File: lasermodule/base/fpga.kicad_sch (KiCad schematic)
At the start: 20 parts, among them U12 ICE40UP5K-SG48ITR-FPGA_Lattice, U13 S25FL064LABMFI010, U14 MCP1700x-120xxTT

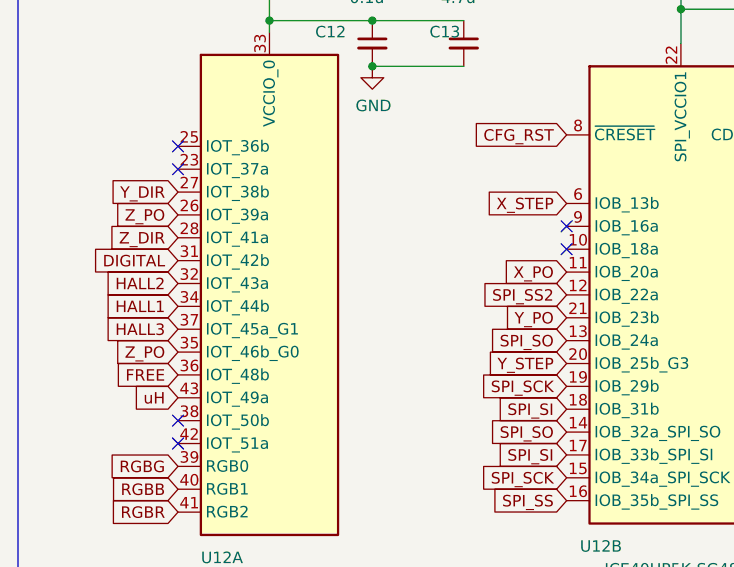
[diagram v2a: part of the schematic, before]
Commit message: flatex cable increased from 15 to 20 pins
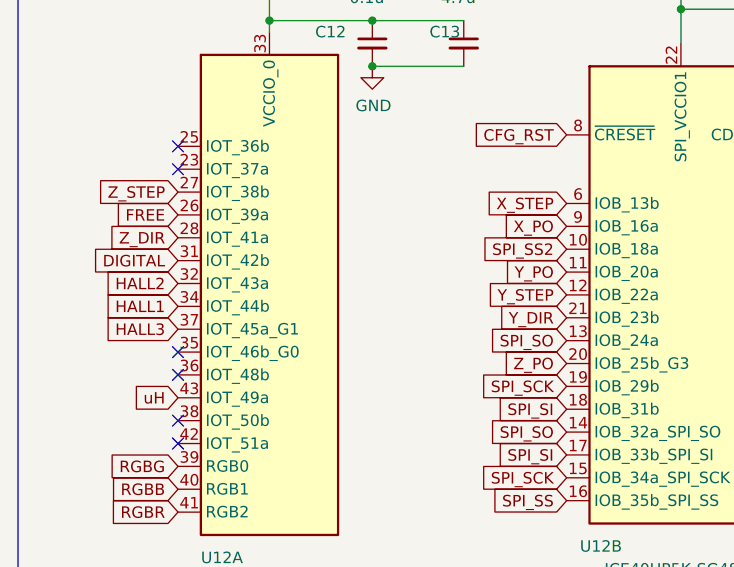
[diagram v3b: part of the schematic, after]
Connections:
- net FREE: now also U12.26 (IOT_39a); no longer U12.36 (IOT_48b)
- net SPI_SS2: now also U12.10 (IOB_18a); no longer U12.12 (IOB_22a)
- net X_PO: now also U12.9 (IOB_16a); no longer U12.11 (IOB_20a)
- net Y_DIR: now also U12.21 (IOB_23b); no longer U12.27 (IOT_38b)
- net Y_PO: now also U12.11 (IOB_20a); no longer U12.21 (IOB_23b)
- net Y_STEP: now also U12.12 (IOB_22a); no longer U12.20 (IOB_25b_G3)
- net Z_PO: now also U12.20 (IOB_25b_G3); no longer U12.26 (IOT_39a), U12.35 (IOT_46b_G0)
- new net Z_STEP: U12.27 (IOT_38b)
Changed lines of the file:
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@@
   )
   (no_connect (at 80.01 54.61))
-  (no_connect (at 123.19 60.96))
+  (no_connect (at 80.01 77.47))
   (no_connect (at 80.01 85.09))
   (no_connect (at 80.01 52.07))
   (no_connect (at 80.01 82.55))
-  (no_connect (at 123.19 63.5))
+  (no_connect (at 80.01 74.93))
   (wire (pts (xy 111.76 43.18) (xy 101.6 43.18))
     (stroke (width 0) (type default))
@@
     (effects (font (size 3 3)) (justify left bottom))
   )
-  (global_label "Y_STEP" (shape input) (at 123.19 76.2 180) (fields_autoplaced)
-    (effects (font (size 1.27 1.27)) (justify right))
-    (property "Intersheetrefs" "${INTERSHEET_REFS}" (at 114.2861 76.2 0)
+  (global_label "Y_STEP" (shape input) (at 123.19 68.58 180) (fields_autoplaced)
+    (effects (font (size 1.27 1.27)) (justify right))
+    (property "Intersheetrefs" "${INTERSHEET_REFS}" (at 114.2861 68.58 0)
       (effects (font (size 1.27 1.27)) (justify right) hide)
     )
@@
     )
   )
-  (global_label "SPI_SS2" (shape input) (at 123.19 68.58 180) (fields_autoplaced)
-    (effects (font (size 1.27 1.27)) (justify right))
-    (property "Intersheetrefs" "${INTERSHEET_REFS}" (at 113.1853 68.5006 0)
+  (global_label "SPI_SS2" (shape input) (at 123.19 63.5 180) (fields_autoplaced)
+    (effects (font (size 1.27 1.27)) (justify right))
+    (property "Intersheetrefs" "${INTERSHEET_REFS}" (at 113.1853 63.4206 0)
       (effects (font (size 1.27 1.27)) (justify right) hide)
     )
@@
     )
   )
-  (global_label "X_PO" (shape input) (at 123.19 66.04 180) (fields_autoplaced)
-    (effects (font (size 1.27 1.27)) (justify right))
-    (property "Intersheetrefs" "${INTERSHEET_REFS}" (at -121.92 6.35 0)
+  (global_label "X_PO" (shape input) (at 123.19 60.96 180) (fields_autoplaced)
+    (effects (font (size 1.27 1.27)) (justify right))
+    (property "Intersheetrefs" "${INTERSHEET_REFS}" (at -121.92 1.27 0)
       (effects (font (size 1.27 1.27)) hide)
     )
@@
     )
   )
-  (global_label "Z_PO" (shape input) (at 80.01 59.69 180) (fields_autoplaced)
-    (effects (font (size 1.27 1.27)) (justify right))
-    (property "Intersheetrefs" "${INTERSHEET_REFS}" (at 72.9808 59.69 0)
+  (global_label "Z_STEP" (shape input) (at 80.01 57.15 180) (fields_autoplaced)
+    (effects (font (size 1.27 1.27)) (justify right))
+    (property "Intersheetrefs" "${INTERSHEET_REFS}" (at 70.9852 57.15 0)
+      (effects (font (size 1.27 1.27)) (justify right) hide)
+    )
+  )
+  (global_label "Z_PO" (shape input) (at 123.19 76.2 180) (fields_autoplaced)
+    (effects (font (size 1.27 1.27)) (justify right))
+    (property "Intersheetrefs" "${INTERSHEET_REFS}" (at 116.1608 76.2 0)
       (effects (font (size 1.27 1.27)) (justify right) hide)
     )
@@
     )
   )
-  (global_label "Z_PO" (shape input) (at 80.01 74.93 180) (fields_autoplaced)
-    (effects (font (size 1.27 1.27)) (justify right))
-    (property "Intersheetrefs" "${INTERSHEET_REFS}" (at 72.9808 74.93 0)
-      (effects (font (size 1.27 1.27)) (justify right) hide)
-    )
-  )
-  (global_label "Y_PO" (shape input) (at 123.19 71.12 180) (fields_autoplaced)
-    (effects (font (size 1.27 1.27)) (justify right))
-    (property "Intersheetrefs" "${INTERSHEET_REFS}" (at 116.2817 71.12 0)
+  (global_label "Y_PO" (shape input) (at 123.19 66.04 180) (fields_autoplaced)
+    (effects (font (size 1.27 1.27)) (justify right))
+    (property "Intersheetrefs" "${INTERSHEET_REFS}" (at 116.2817 66.04 0)
       (effects (font (size 1.27 1.27)) (justify right) hide)
     )
@@
     (effects (font (size 1.27 1.27)) (justify right))
     (property "Intersheetrefs" "${INTERSHEET_REFS}" (at 72.4365 62.23 0)
-      (effects (font (size 1.27 1.27)) (justify right) hide)
-    )
-  )
-  (global_label "FREE" (shape input) (at 80.01 77.47 180) (fields_autoplaced)
-    (effects (font (size 1.27 1.27)) (justify right))
-    (property "Intersheetrefs" "${INTERSHEET_REFS}" (at 73.1018 77.47 0)
       (effects (font (size 1.27 1.27)) (justify right) hide)
     )
@@
     )
   )
+  (global_label "FREE" (shape input) (at 80.01 59.69 180) (fields_autoplaced)
+    (effects (font (size 1.27 1.27)) (justify right))
+    (property "Intersheetrefs" "${INTERSHEET_REFS}" (at 73.1018 59.69 0)
+      (effects (font (size 1.27 1.27)) (justify right) hide)
+    )
+  )
   (global_label "CFG_DONE" (shape input) (at 168.91 59.69 0) (fields_autoplaced)
     (effects (font (size 1.27 1.27)) (justify left))
@@
     )
   )
-  (global_label "Y_DIR" (shape input) (at 80.01 57.15 180) (fields_autoplaced)
-    (effects (font (size 1.27 1.27)) (justify right))
-    (property "Intersheetrefs" "${INTERSHEET_REFS}" (at 72.5574 57.15 0)
-      (effects (font (size 1.27 1.27)) (justify right) hide)
-    )
+  (global_label "Y_DIR" (shape input) (at 123.19 71.12 180) (fields_autoplaced)
+    (effects (font (size 1.27 1.27)) (justify right))
+    (property "Intersheetrefs" "${INTERSHEET_REFS}" (at 115.7374 71.12 0)
+      (effects (font (size 1.27 1.27)) (justify right) hide)
+    )

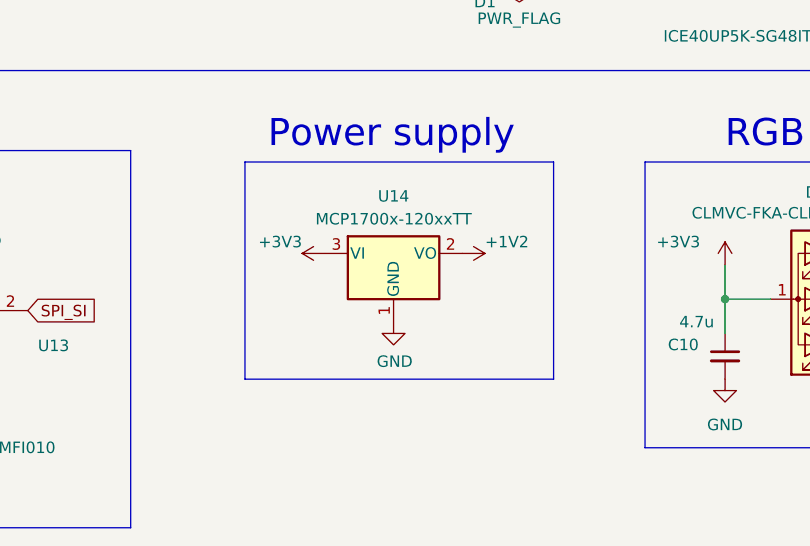
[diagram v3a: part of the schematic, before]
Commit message: started routing main board with esp32
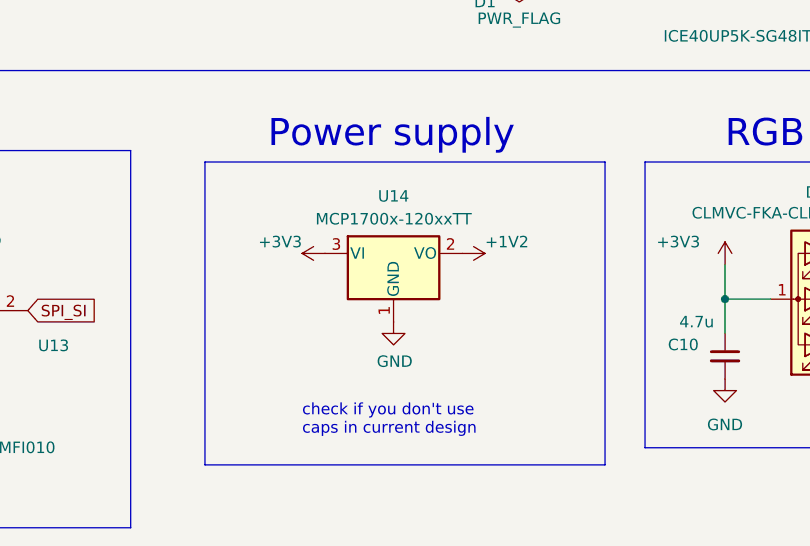
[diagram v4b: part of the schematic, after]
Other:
- note added: "check if you don't use caps in current design"
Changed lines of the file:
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@@
     (stroke (width 0) (type default))
   )
-  (polyline (pts (xy 189.23 132.08) (xy 189.23 156.21))
+  (polyline (pts (xy 194.945 132.08) (xy 194.945 165.735))
     (stroke (width 0) (type default))
   )
@@
     (stroke (width 0) (type default))
   )
-  (polyline (pts (xy 154.94 156.21) (xy 154.94 132.08))
+  (polyline (pts (xy 150.495 165.735) (xy 150.495 132.08))
     (stroke (width 0) (type default))
   )
@@
     (stroke (width 0) (type default))
   )
-  (polyline (pts (xy 154.94 132.08) (xy 189.23 132.08))
+  (polyline (pts (xy 150.495 132.08) (xy 194.945 132.08))
     (stroke (width 0) (type default))
   )
@@
     (stroke (width 0) (type default))
   )
-  (polyline (pts (xy 189.23 156.21) (xy 154.94 156.21))
+  (polyline (pts (xy 194.945 165.735) (xy 150.495 165.735))
     (stroke (width 0) (type default))
   )
@@
     (effects (font (size 3 3)) (justify left bottom))
   )
+  (text "check if you don't use \ncaps in current design" (at 161.29 162.56 0)
+    (effects (font (size 1.27 1.27)) (justify left bottom))
+  )
   (text "Memory" (at 96.52 129.54 0)
